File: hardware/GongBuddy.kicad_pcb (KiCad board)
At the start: 4 copper layers, 39 x 59 mm, 62 parts, among them J1 10103594-0001LF, J2 Conn_ARM_JTAG_SWD_10, J3 2908-05WB-MG, J4 Conn_01x10, J5 Conn_01x02, J7 Conn_Coaxial, U1 TPS7A19, U2 USBLC6-2SC6, U3 MCP73831T-2ACI_OT, U4 ST_Sensortile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

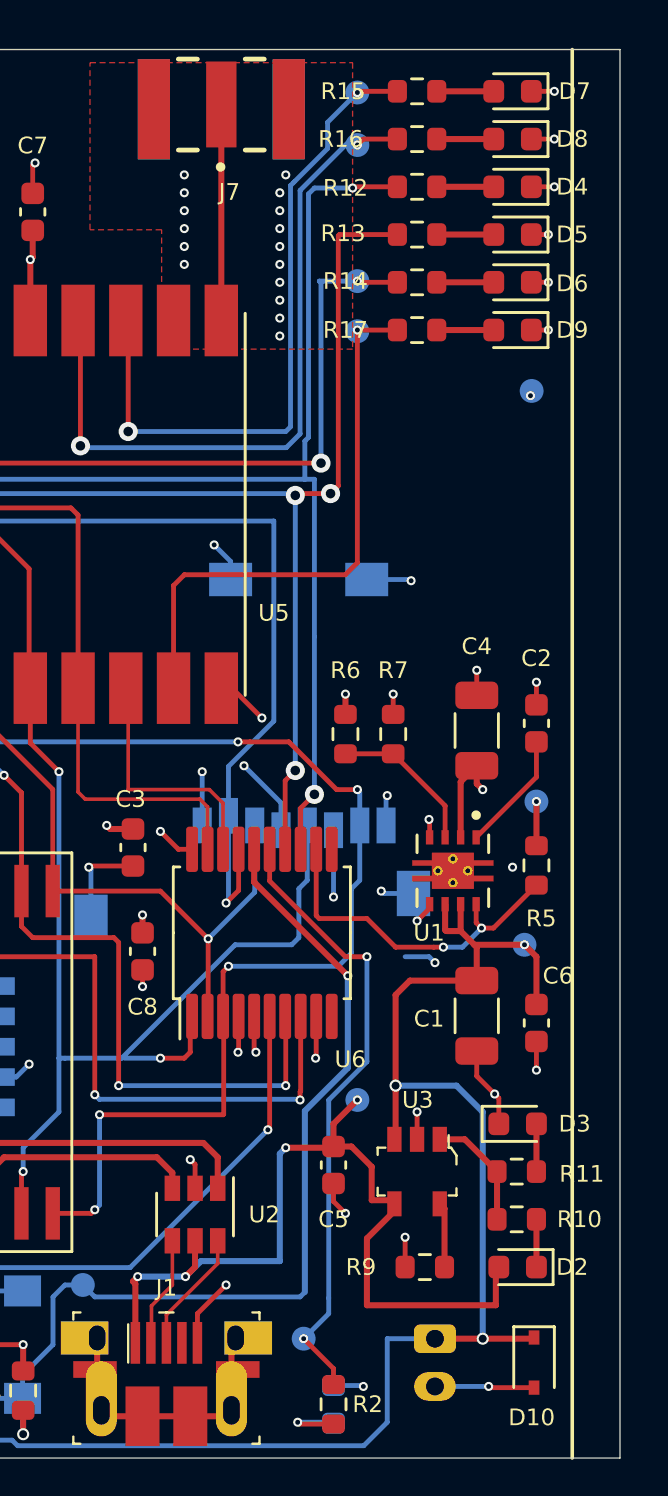
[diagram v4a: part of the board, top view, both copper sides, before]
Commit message: Tweaked the RF lines.
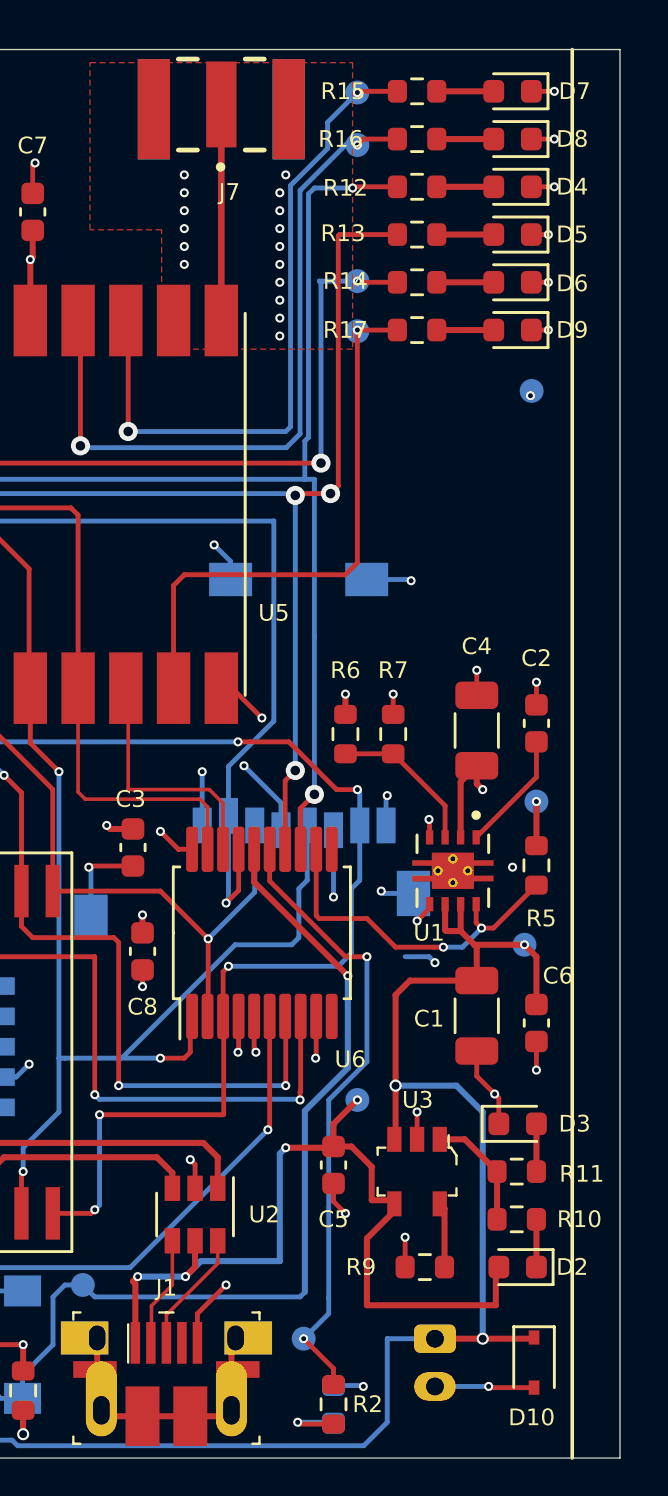
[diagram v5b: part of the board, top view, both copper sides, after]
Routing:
- added copper zone on In1.Cu, net GND
- added copper zone on In2.Cu, net VCC
- removed copper zone on In2.Cu, net GND
- removed copper zone on In1.Cu, net VCC
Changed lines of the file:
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@@
       (outputformat 1)
       (mirror false)
-      (drillshape 1)
+      (drillshape 0)
       (scaleselection 1)
-      (outputdirectory ""))
+      (outputdirectory "gerber"))
   )
   (net 0 "")
@@
       (effects (font (size 0.9906 0.9906) (thickness 0.2286)))
     )
-    (pad 2 smd roundrect (at 1.475 0 90) (size 1.15 1.8) (layers F.Cu F.Paste F.Mask) (roundrect_rratio 0.217391)
+    (pad 2 smd roundrect (at 1.475 0 90) (size 1.15 1.8) (layers F.Cu F.Paste F.Mask) (roundrect_rratio 0.2173904347826087)
       (net 1 GND))
-    (pad 1 smd roundrect (at -1.475 0 90) (size 1.15 1.8) (layers F.Cu F.Paste F.Mask) (roundrect_rratio 0.217391)
+    (pad 1 smd roundrect (at -1.475 0 90) (size 1.15 1.8) (layers F.Cu F.Paste F.Mask) (roundrect_rratio 0.2173904347826087)
       (net 4 VCC))
     (model ${KISYS3DMOD}/Capacitor_SMD.3dshapes/C_1206_3216Metric.wrl
@@
       (effects (font (size 0.9906 0.9906) (thickness 0.2286)))
     )
-    (pad 2 smd roundrect (at 1.475 0 270) (size 1.15 1.8) (layers F.Cu F.Paste F.Mask) (roundrect_rratio 0.217391)
+    (pad 2 smd roundrect (at 1.475 0 270) (size 1.15 1.8) (layers F.Cu F.Paste F.Mask) (roundrect_rratio 0.2173904347826087)
       (net 1 GND))
-    (pad 1 smd roundrect (at -1.475 0 270) (size 1.15 1.8) (layers F.Cu F.Paste F.Mask) (roundrect_rratio 0.217391)
+    (pad 1 smd roundrect (at -1.475 0 270) (size 1.15 1.8) (layers F.Cu F.Paste F.Mask) (roundrect_rratio 0.2173904347826087)
       (net 2 /VBAT))
     (model ${KISYS3DMOD}/Capacitor_SMD.3dshapes/C_1206_3216Metric.wrl
@@
     (pad 2 thru_hole oval (at 2 0 270) (size 1.2 1.75) (drill 0.75) (layers *.Cu *.Mask)
       (net 1 GND))
-    (pad 1 thru_hole roundrect (at 0 0 270) (size 1.2 1.75) (drill 0.75) (layers *.Cu *.Mask) (roundrect_rratio 0.208333)
+    (pad 1 thru_hole roundrect (at 0 0 270) (size 1.2 1.75) (drill 0.75) (layers *.Cu *.Mask) (roundrect_rratio 0.2083325)
       (net 2 /VBAT))
     (model ${KISYS3DMOD}/Connector_JST.3dshapes/JST_PH_B2B-PH-K_1x02_P2.00mm_Vertical.wrl
@@
   (segment (start 67.675 85.75) (end 65.85 85.75) (width 0.2032) (layer F.Cu) (net 29))
   (via (at 65.8 85.8) (size 0.381) (drill 0.2032) (layers F.Cu B.Cu) (net 29))
-  (segment (start 60.3 91.35) (end 60.3 82.3) (width 0.254) (layer F.Cu) (net 30))
+  (segment (start 60.3 91.35) (end 60.3 82.3) (width 0.28) (layer F.Cu) (net 30))
   (segment (start 64.275 113.5) (end 64.275 116.275) (width 0.2032) (layer F.Cu) (net 31))
   (segment (start 64.275 116.275) (end 64.4 116.4) (width 0.2032) (layer F.Cu) (net 31))
@@
     )
   )
-  (zone (net 1) (net_name GND) (layer In2.Cu) (hatch edge 0.508)
+  (zone (net 1) (net_name GND) (layer In1.Cu) (hatch edge 0.508)
     (connect_pads (clearance 0.1542))
     (min_thickness 0.254)
@@
     )
   )
-  (zone (net 4) (net_name VCC) (layer In1.Cu) (hatch edge 0.508)
+  (zone (net 4) (net_name VCC) (layer In2.Cu) (hatch edge 0.508)
     (connect_pads (clearance 0.1542))
     (min_thickness 0.254)
